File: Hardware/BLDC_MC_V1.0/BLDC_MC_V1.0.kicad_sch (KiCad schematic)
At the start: 0 parts

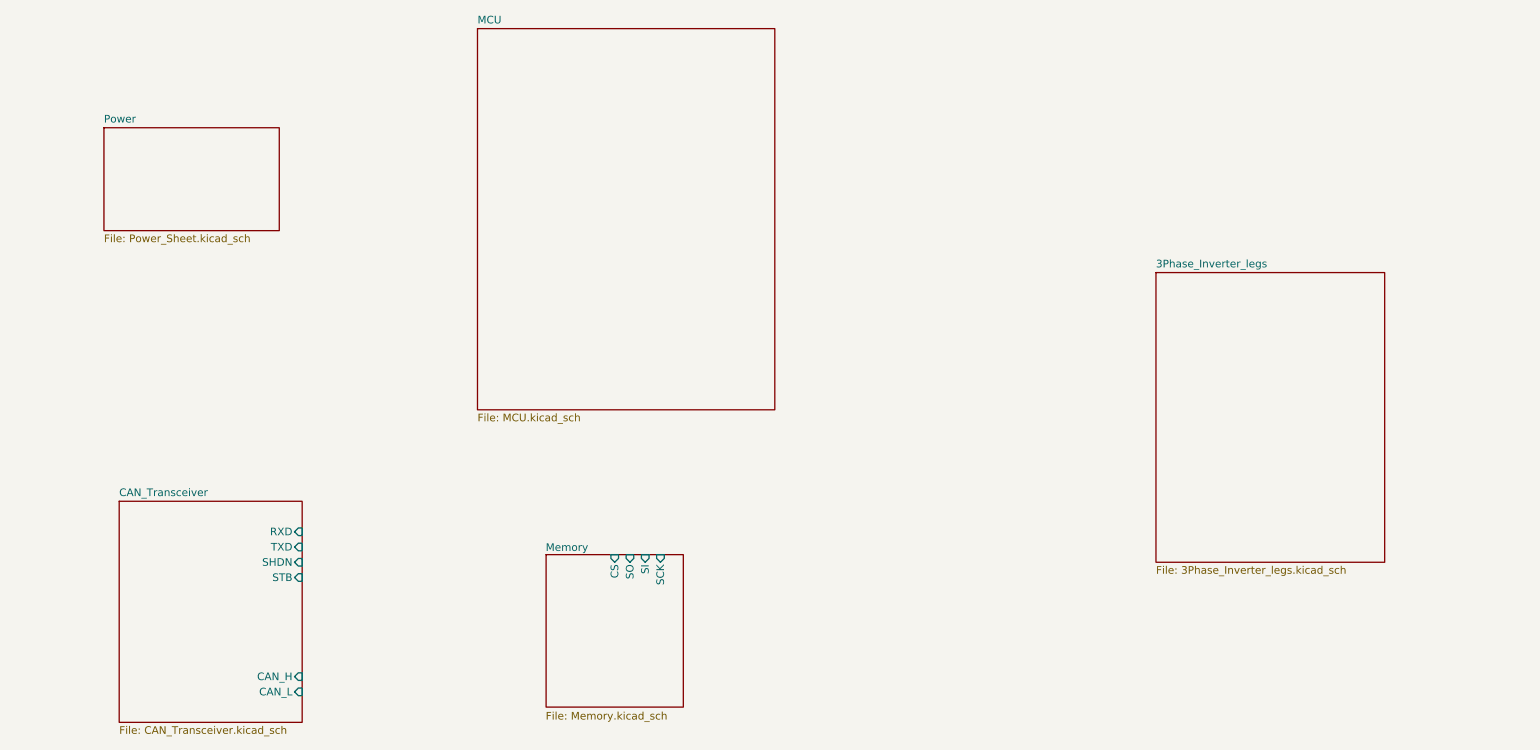
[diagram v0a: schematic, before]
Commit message: Rename the project files to take version name
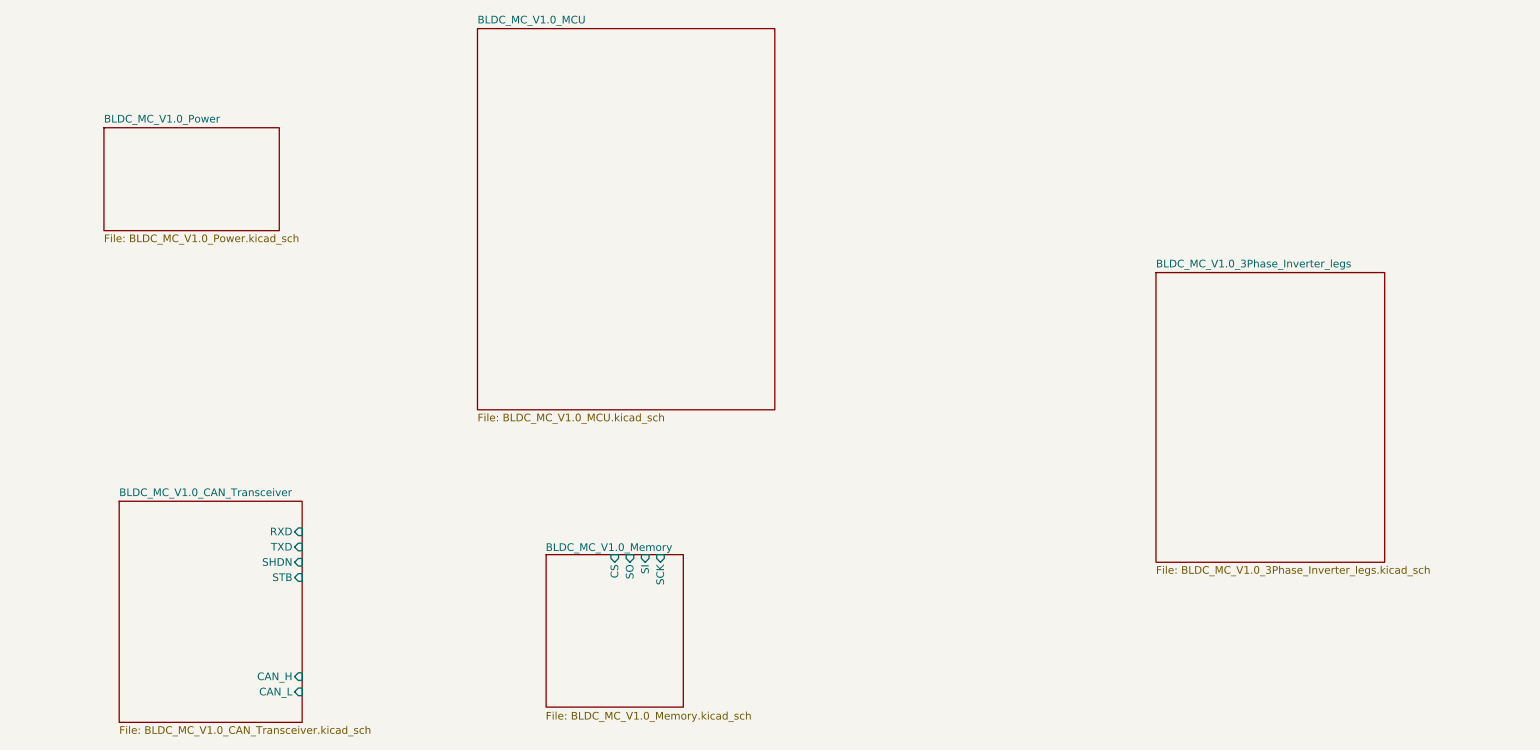
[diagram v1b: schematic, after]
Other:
- sheet 3Phase_Inverter_legs renamed BLDC_MC_V1.0_3Phase_Inverter_legs
- sheet CAN_Transceiver renamed BLDC_MC_V1.0_CAN_Transceiver
- sheet MCU renamed BLDC_MC_V1.0_MCU
- sheet Memory renamed BLDC_MC_V1.0_Memory
- sheet Power renamed BLDC_MC_V1.0_Power
- sheet BLDC_MC_V1.0_3Phase_Inverter_legs: file 3Phase_Inverter_legs.kicad_sch -> BLDC_MC_V1.0_3Phase_Inverter_legs.kicad_sch
- sheet BLDC_MC_V1.0_CAN_Transceiver: file CAN_Transceiver.kicad_sch -> BLDC_MC_V1.0_CAN_Transceiver.kicad_sch
- sheet BLDC_MC_V1.0_MCU: file MCU.kicad_sch -> BLDC_MC_V1.0_MCU.kicad_sch
- sheet BLDC_MC_V1.0_Memory: file Memory.kicad_sch -> BLDC_MC_V1.0_Memory.kicad_sch
- sheet BLDC_MC_V1.0_Power: file Power_Sheet.kicad_sch -> BLDC_MC_V1.0_Power.kicad_sch
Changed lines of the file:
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@@
 			(color 0 0 0 0.0000)
 		)
-		(property "Sheetname" "CAN_Transceiver"
+		(property "Sheetname" "BLDC_MC_V1.0_CAN_Transceiver"
 			(at 44.45 118.6684 0)
 			(effects
@@
 			)
 		)
-		(property "Sheetfile" "CAN_Transceiver.kicad_sch"
+		(property "Sheetfile" "BLDC_MC_V1.0_CAN_Transceiver.kicad_sch"
 			(at 44.45 156.7946 0)
 			(effects
@@
 		)
 		(instances
-			(project "BLDC_Motor_Driver"
+			(project "BLDC_MC_V1.0"
 				(path "/e34fda66-7244-4ac9-bbf7-3725f03e688f"
 					(page "4")
@@
 			(color 0 0 0 0.0000)
 		)
-		(property "Sheetname" "3Phase_Inverter_legs"
+		(property "Sheetname" "BLDC_MC_V1.0_3Phase_Inverter_legs"
 			(at 217.17 80.5684 0)
 			(effects
@@
 			)
 		)
-		(property "Sheetfile" "3Phase_Inverter_legs.kicad_sch"
+		(property "Sheetfile" "BLDC_MC_V1.0_3Phase_Inverter_legs.kicad_sch"
 			(at 217.17 130.1246 0)
 			(effects
@@
 		)
 		(instances
-			(project "BLDC_Motor_Driver"
+			(project "BLDC_MC_V1.0"
 				(path "/e34fda66-7244-4ac9-bbf7-3725f03e688f"
 					(page "6")
@@
 			(color 0 0 0 0.0000)
 		)
-		(property "Sheetname" "MCU"
+		(property "Sheetname" "BLDC_MC_V1.0_MCU"
 			(at 104.14 39.9284 0)
 			(effects
@@
 			)
 		)
-		(property "Sheetfile" "MCU.kicad_sch"
+		(property "Sheetfile" "BLDC_MC_V1.0_MCU.kicad_sch"
 			(at 104.14 104.7246 0)
 			(effects
@@
 		)
 		(instances
-			(project "BLDC_Motor_Driver"
+			(project "BLDC_MC_V1.0"
 				(path "/e34fda66-7244-4ac9-bbf7-3725f03e688f"
 					(page "3")
@@
 			(color 0 0 0 0.0000)
 		)
-		(property "Sheetname" "Memory"
+		(property "Sheetname" "BLDC_MC_V1.0_Memory"
 			(at 115.5043 127.8101 0)
 			(effects
@@
 			)
 		)
-		(property "Sheetfile" "Memory.kicad_sch"
+		(property "Sheetfile" "BLDC_MC_V1.0_Memory.kicad_sch"
 			(at 115.5043 154.4144 0)
 			(effects
@@
 		)
 		(instances
-			(project "BLDC_Motor_Driver"
+			(project "BLDC_MC_V1.0"
 				(path "/e34fda66-7244-4ac9-bbf7-3725f03e688f"
 					(page "5")
@@
 			(color 0 0 0 0.0000)
 		)
-		(property "Sheetname" "Power"
+		(property "Sheetname" "BLDC_MC_V1.0_Power"
 			(at 41.91 56.4384 0)
 			(effects
@@
 			)
 		)
-		(property "Sheetfile" "Power_Sheet.kicad_sch"
+		(property "Sheetfile" "BLDC_MC_V1.0_Power.kicad_sch"
 			(at 41.91 74.8796 0)
 			(effects
@@
 		)
 		(instances
-			(project "BLDC_Motor_Driver"
+			(project "BLDC_MC_V1.0"
 				(path "/e34fda66-7244-4ac9-bbf7-3725f03e688f"
 					(page "2")

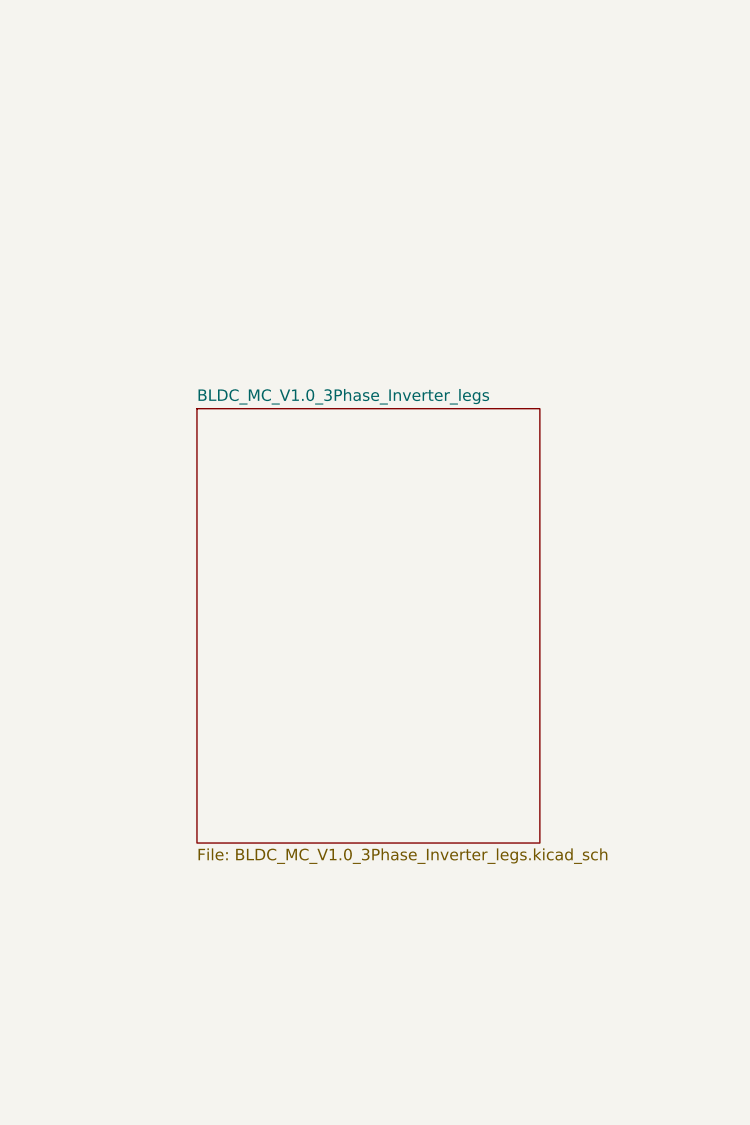
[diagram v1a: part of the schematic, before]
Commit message: Add datasheet and library of DVR (gate drive IC) and add the sheet of gate drive circuit
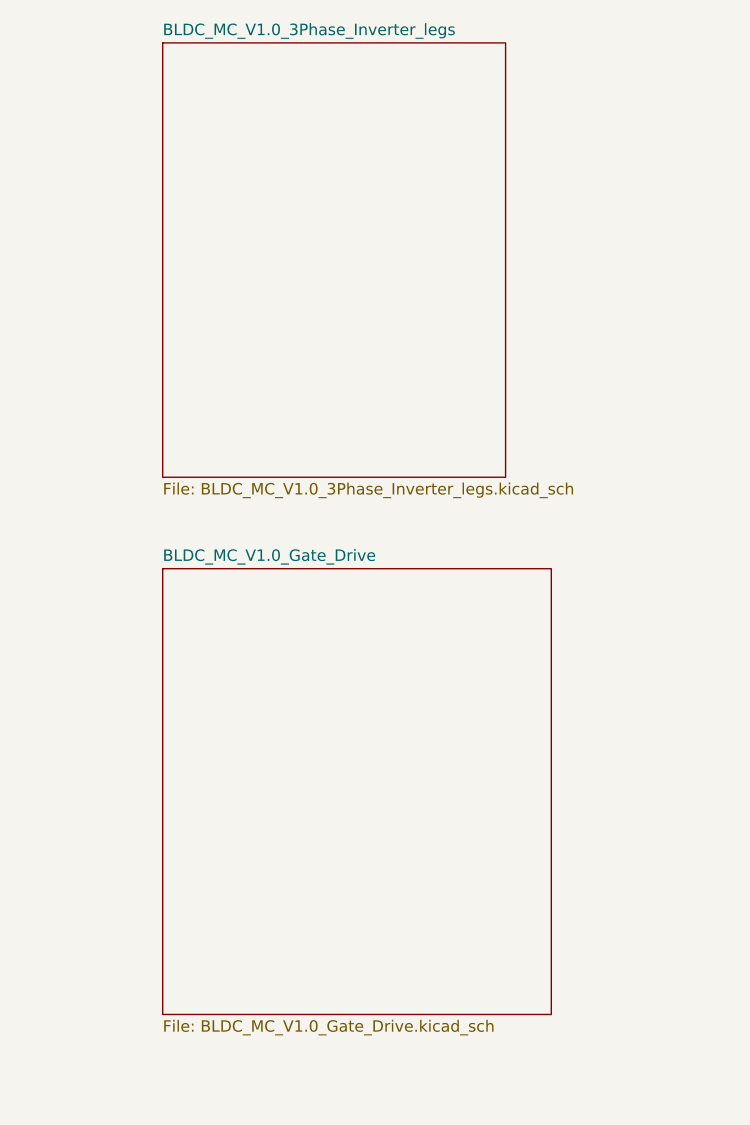
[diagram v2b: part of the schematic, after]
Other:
- added sheet BLDC_MC_V1.0_Gate_Drive (BLDC_MC_V1.0_Gate_Drive.kicad_sch)
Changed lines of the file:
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@@
 	)
 	(sheet
-		(at 217.17 81.28)
+		(at 213.36 99.06)
+		(size 43.18 49.53)
+		(exclude_from_sim no)
+		(in_bom yes)
+		(on_board yes)
+		(dnp no)
+		(fields_autoplaced yes)
+		(stroke
+			(width 0.1524)
+			(type solid)
+		)
+		(fill
+			(color 0 0 0 0.0000)
+		)
+		(property "Sheetname" "BLDC_MC_V1.0_Gate_Drive"
+			(at 213.36 98.3484 0)
+			(effects
+				(font
+					(size 1.27 1.27)
+				)
+				(justify left bottom)
+			)
+		)
+		(property "Sheetfile" "BLDC_MC_V1.0_Gate_Drive.kicad_sch"
+			(at 213.36 149.1746 0)
+			(effects
+				(font
+					(size 1.27 1.27)
+				)
+				(justify left top)
+			)
+		)
+		(instances
+			(project "BLDC_MC_V1.0"
+				(path "/e34fda66-7244-4ac9-bbf7-3725f03e688f"
+					(page "7")
+				)
+			)
+		)
+	)
+	(sheet
+		(at 213.36 40.64)
 		(size 38.1 48.26)
 		(exclude_from_sim no)
@@
 		)
 		(property "Sheetname" "BLDC_MC_V1.0_3Phase_Inverter_legs"
-			(at 217.17 80.5684 0)
+			(at 213.36 39.9284 0)
 			(effects
 				(font
@@
 		)
 		(property "Sheetfile" "BLDC_MC_V1.0_3Phase_Inverter_legs.kicad_sch"
-			(at 217.17 130.1246 0)
+			(at 213.36 89.4846 0)
 			(effects
 				(font

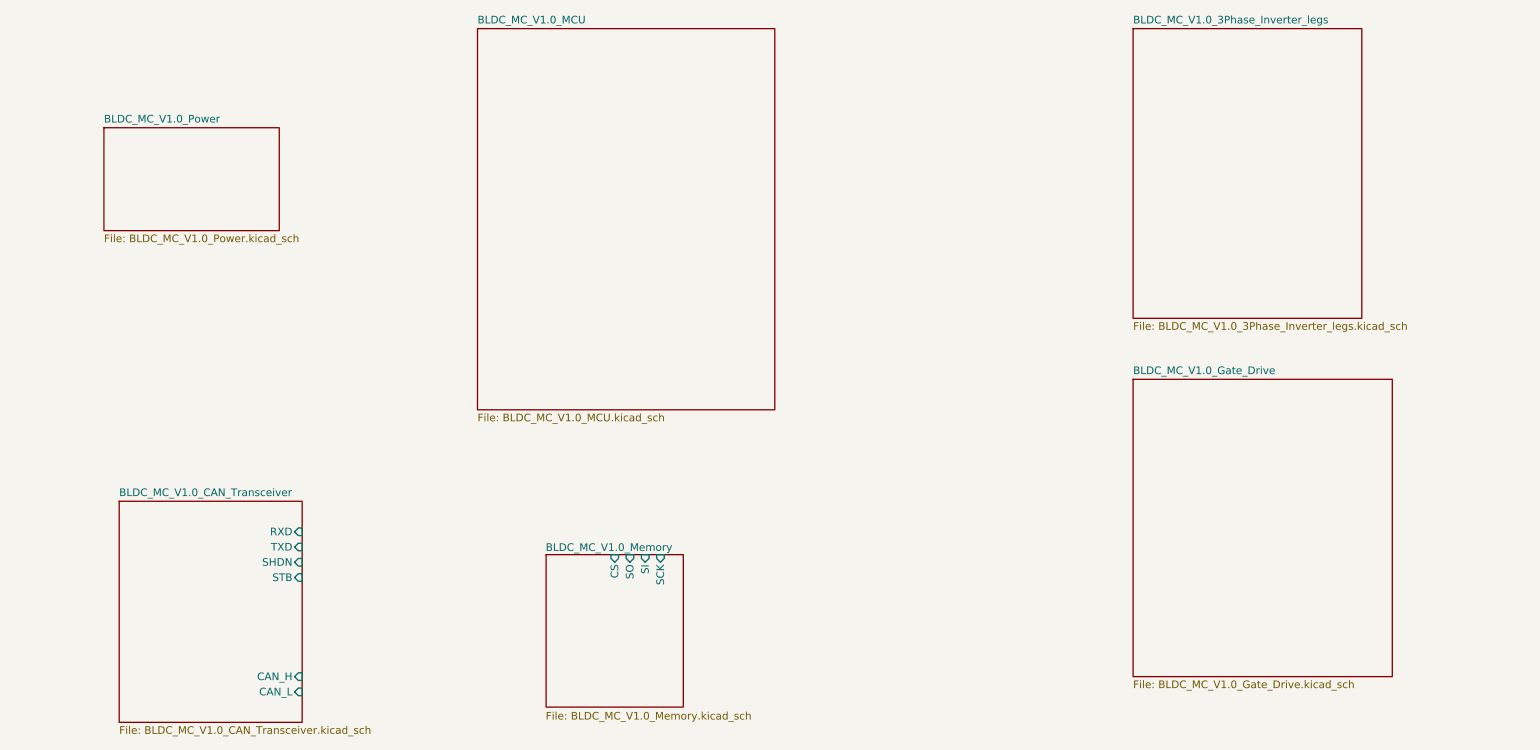
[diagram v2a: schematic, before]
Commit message: Edit the connection between sheets and add some details and connections to gatedrive sheet
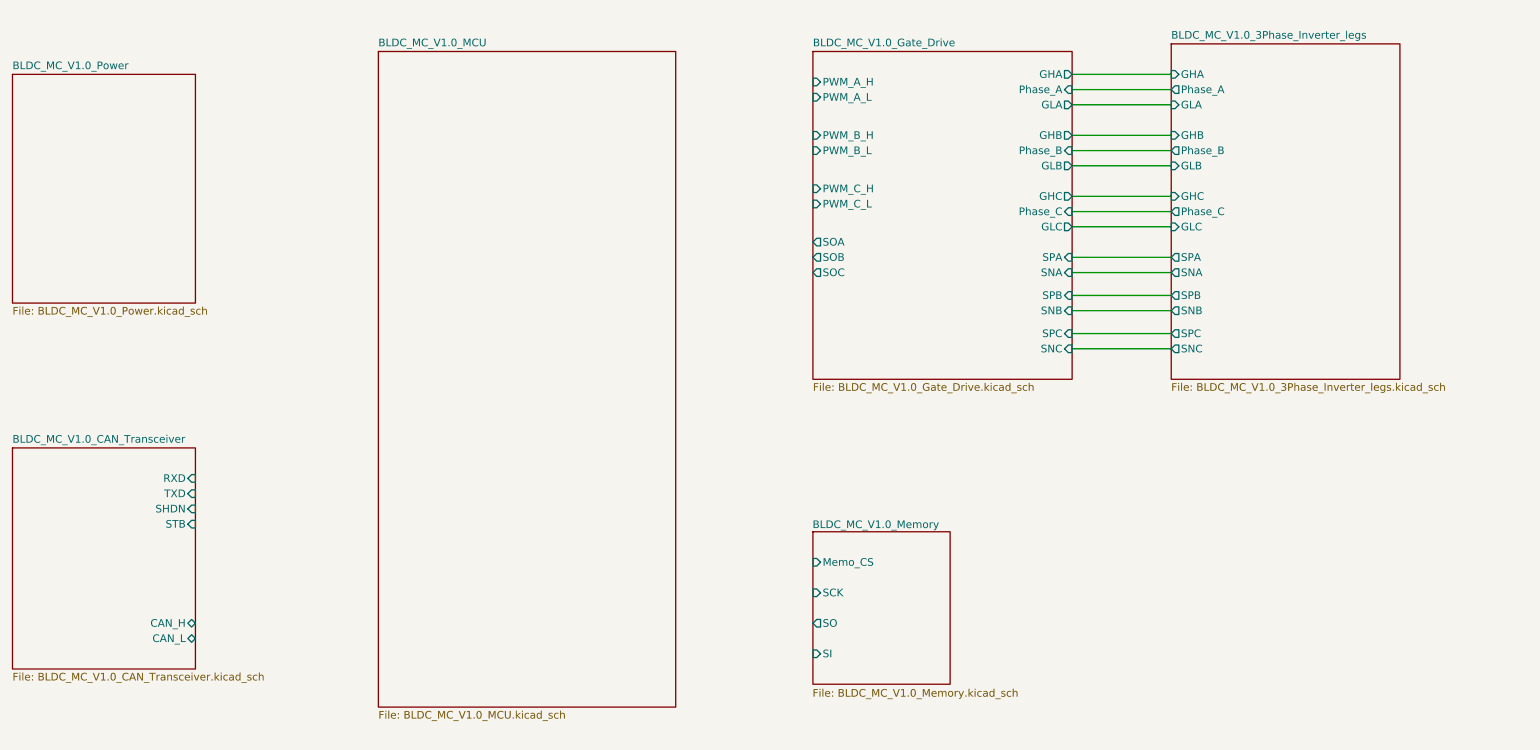
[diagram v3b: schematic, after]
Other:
- sheet BLDC_MC_V1.0_3Phase_Inverter_legs ports: added GHA, GHB, GHC, GLA, GLB, GLC, Phase_A, Phase_B, Phase_C, SNA, SNB, SNC, SPA, SPB, SPC; removed none
- sheet BLDC_MC_V1.0_Gate_Drive ports: added GHA, GHB, GHC, GLA, GLB, GLC, PWM_A_H, PWM_A_L, PWM_B_H, PWM_B_L, PWM_C_H, PWM_C_L, Phase_A, Phase_B, Phase_C, SNA, SNB, SNC, SOA, SOB, SOC, SPA, SPB, SPC; removed none
- sheet BLDC_MC_V1.0_Memory ports: added Memo_CS; removed CS

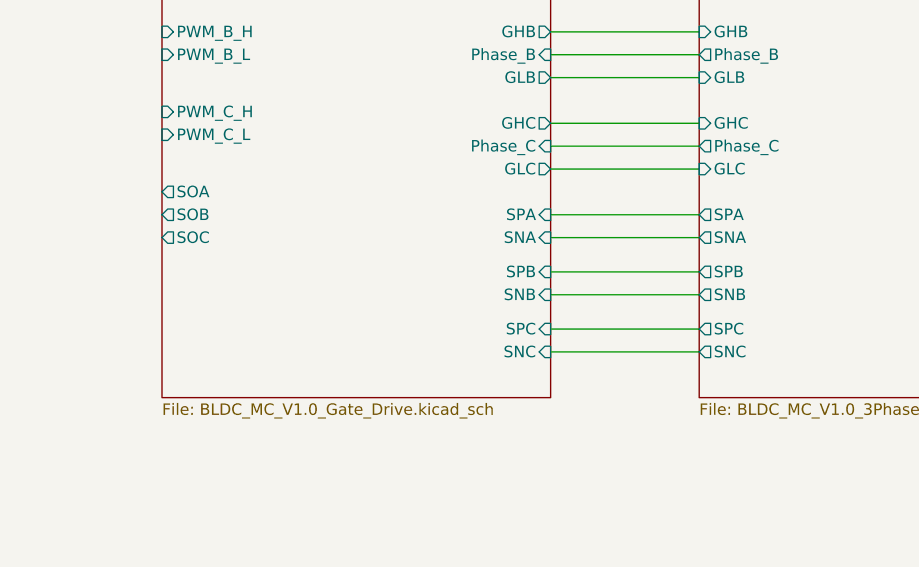
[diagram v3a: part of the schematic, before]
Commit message: Restore the importenat project files from last commit and define the routing of current sensor as differntial pair
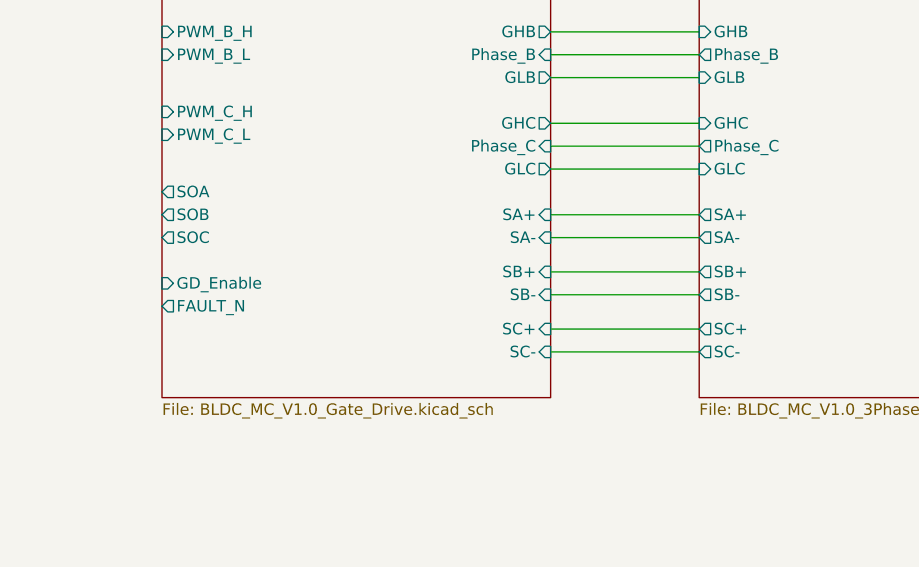
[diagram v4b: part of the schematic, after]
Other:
- sheet BLDC_MC_V1.0_3Phase_Inverter_legs ports: added SA+, SA-, SB+, SB-, SC+, SC-; removed SNA, SNB, SNC, SPA, SPB, SPC
- sheet BLDC_MC_V1.0_Gate_Drive ports: added FAULT_N, GD_Enable, SA+, SA-, SB+, SB-, SC+, SC-; removed SNA, SNB, SNC, SPA, SPB, SPC
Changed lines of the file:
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@@
 			)
 		)
-		(pin "SPA" input
+		(pin "SA+" input
 			(at 203.2 78.74 0)
 			(effects
@@
 			)
 		)
-		(pin "SNC" input
+		(pin "SC-" input
 			(at 203.2 93.98 0)
 			(effects
@@
 			)
 		)
-		(pin "SNB" input
+		(pin "SB-" input
 			(at 203.2 87.63 0)
 			(effects
@@
 			)
 		)
-		(pin "SPB" input
+		(pin "SB+" input
 			(at 203.2 85.09 0)
 			(effects
@@
 			)
 		)
-		(pin "SPC" input
+		(pin "SC+" input
 			(at 203.2 91.44 0)
 			(effects
@@
 			)
 		)
-		(pin "SNA" input
+		(pin "SA-" input
 			(at 203.2 81.28 0)
 			(effects
@@
 				)
 				(justify right)
+			)
+		)
+		(pin "GD_Enable" input
+			(at 160.02 86.36 180)
+			(effects
+				(font
+					(size 1.27 1.27)
+				)
+				(justify left)
+			)
+		)
+		(pin "FAULT_N" output
+			(at 160.02 88.9 180)
+			(effects
+				(font
+					(size 1.27 1.27)
+				)
+				(justify left)
 			)
 		)
@@
 			)
 		)
-		(pin "SPC" output
+		(pin "SC+" output
 			(at 219.71 91.44 180)
 			(effects
@@
 			)
 		)
-		(pin "SNC" output
+		(pin "SC-" output
 			(at 219.71 93.98 180)
 			(effects
@@
 			)
 		)
-		(pin "SNA" output
+		(pin "SA-" output
 			(at 219.71 81.28 180)
 			(effects
@@
 			)
 		)
-		(pin "SPB" output
+		(pin "SB+" output
 			(at 219.71 85.09 180)
 			(effects
@@
 			)
 		)
-		(pin "SNB" output
+		(pin "SB-" output
 			(at 219.71 87.63 180)
 			(effects
@@
 			)
 		)
-		(pin "SPA" output
+		(pin "SA+" output
 			(at 219.71 78.74 180)
 			(effects
